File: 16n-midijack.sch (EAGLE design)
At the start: 28 parts

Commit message: Everything on the board.
Now needs routing. Oh boy.
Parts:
- added C1, C2, C3, C4, C5, C6, C7, C8: 100n, rcl:C-EUC0805
- added J1, J10, J11, J12, J13, J14, J15, J16, J2, J3, J4, J5, J6, J7, J8, J9: THONKICONNNEW, MusicThingModular:THONKICONNNEW
- added R10, R14, R15, R19, R20, R24, R25, R29, R30, R34, R35, R39, R40, R44, R5, R9: 5.6K, rcl:R-EU_R0805
- added R11, R13, R16, R18, R21, R23, R26, R28, R31, R33, R36, R38, R41, R43, R6, R8: 10K, rcl:R-EU_R0805
- added R12, R17, R22, R27, R32, R37, R42, R45, R46, R47, R48, R49, R50, R51, R52, R7: 100, rcl:R-EU_R0805
- added U1, U2, U3, U4, U5, U6, U7, U8: MCP6004_SMD, MusicThingModular:MCP6004_SMD
- D1, D2, D3, D4: value DIODE-1N4148 -> DIODESOD123; device SparkFun-DiscreteSemi:DIODE-1N4148 -> foxfield:DIODESOD123
- R1, R2: value (none) -> 220; device SparkFun-Resistors:RESISTORAXIAL-0.3-KIT -> rcl:R-EU_R0805
- R3, R4: device SparkFun-Resistors:RESISTORAXIAL-0.3-KIT -> rcl:R-EU_R0805
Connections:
- new net CV1: J1.TIP, R7.2
- new net CV10: J10.TIP, R48.2
- new net CV11: J11.TIP, R32.2
- new net CV12: J12.TIP, R49.2
- new net CV13: J13.TIP, R37.2
- new net CV14: J14.TIP, R50.2
- new net CV15: J15.TIP, R42.2
- new net CV16: J16.TIP, R51.2
- new net CV2: J2.TIP, R12.2
- new net CV3: J3.TIP, R52.2
- new net CV4: J4.TIP, R45.2
- new net CV5: J5.TIP, R17.2
- new net CV6: J6.TIP, R47.2
- new net CV7: J7.TIP, R22.2
- new net CV8: J8.TIP, R46.2
- new net CV9: J9.TIP, R27.2
- new net N$10: R8.2, R9.2, U1D.+IN
- new net N$11: R17.1, U3C.-IN, U3C.OUT
- new net N$12: R15.2, R16.2, U3C.+IN
- new net N$13: R18.2, R19.2, U3D.+IN
- new net N$14: R22.1, U4C.-IN, U4C.OUT
- new net N$15: R20.2, R21.2, U4C.+IN
- new net N$16: R23.2, R24.2, U4D.+IN
- new net N$17: R27.1, U5C.-IN, U5C.OUT
- new net N$18: R25.2, R26.2, U5C.+IN
- new net N$19: R28.2, R29.2, U5D.+IN
- new net N$20: R32.1, U6C.-IN, U6C.OUT
- new net N$21: R30.2, R31.2, U6C.+IN
- new net N$22: R33.2, R34.2, U6D.+IN
- new net N$23: R37.1, U7C.-IN, U7C.OUT
- new net N$24: R35.2, R36.2, U7C.+IN
- new net N$25: R38.2, R39.2, U7D.+IN
- new net N$256: R12.1, U1D.-IN, U1D.OUT
- new net N$257: R45.1, U2D.-IN, U2D.OUT
- new net N$258: R47.1, U3D.-IN, U3D.OUT
- new net N$259: R46.1, U4D.-IN, U4D.OUT
- new net N$26: R42.1, U8C.-IN, U8C.OUT
- new net N$260: R48.1, U5D.-IN, U5D.OUT
- new net N$261: R49.1, U6D.-IN, U6D.OUT
- new net N$262: R50.1, U7D.-IN, U7D.OUT
- new net N$263: R51.1, U8D.-IN, U8D.OUT
- new net N$27: R40.2, R41.2, U8C.+IN
- new net N$28: R43.2, R44.2, U8D.+IN
- new net N$5: R52.1, U2C.-IN, U2C.OUT
- new net N$6: R10.2, R11.2, U2C.+IN
- new net N$7: R13.2, R14.2, U2D.+IN
- new net N$8: R7.1, U1C.-IN, U1C.OUT
- new net N$9: R5.2, R6.2, U1C.+IN
- new net W0: R5.1, U$17.2, U1B.+IN
- new net W1: R9.1, U$16.2, U1A.+IN
- new net W10: R30.1, U$7.2, U6B.+IN
- new net W11: R34.1, U$6.2, U6A.+IN
- new net W12: R35.1, U$5.2, U7B.+IN
- new net W13: R39.1, U$4.2, U7A.+IN
- new net W14: R40.1, U$3.2, U8B.+IN
- new net W15: R44.1, U$2.2, U8A.+IN
- new net W2: R10.1, U$15.2, U2B.+IN
- new net W3: R14.1, U$14.2, U2A.+IN
- new net W4: R15.1, U$13.2, U3B.+IN
- new net W5: R19.1, U$12.2, U3A.+IN
- new net W6: R20.1, U$11.2, U4B.+IN
- new net W7: R24.1, U$10.2, U4A.+IN
- new net W8: R25.1, U$9.2, U5B.+IN
- new net W9: R29.1, U$8.2, U5A.+IN
- net +3V3: no longer U$10.1, U$11.1, U$12.1, U$13.1, U$14.1, U$15.1, U$16.1, U$17.1, U$2.1, U$3.1, U$4.1, U$5.1, U$6.1, U$7.1, U$8.1, U$9.1
- net +5V: now also C1.1, C2.1, C3.1, C4.1, C5.1, C6.1, C7.1, C8.1, U$10.1, U$11.1, U$12.1, U$13.1, U$14.1, U$15.1, U$16.1, U$17.1, U$2.1, U$3.1, U$4.1, U$5.1, U$6.1, U$7.1, U$8.1, U$9.1, U1P.V+, U2P.V+, U3P.V+, U4P.V+, U5P.V+, U6P.V+, U7P.V+, U8P.V+
- net A0: now also U1B.-IN, U1B.OUT; no longer U$2.2
- net A1: now also U1A.-IN, U1A.OUT; no longer U$3.2
- net A10: now also U6B.-IN, U6B.OUT; no longer U$12.2
- net A11: now also U6A.-IN, U6A.OUT; no longer U$13.2
- net A12: now also U7B.-IN, U7B.OUT; no longer U$14.2
- net A13: now also U7A.-IN, U7A.OUT; no longer U$15.2
- net A14: now also U8B.-IN, U8B.OUT; no longer U$16.2
- net A15: now also U8A.-IN, U8A.OUT; no longer U$17.2
- net A2: now also U2B.-IN, U2B.OUT; no longer U$4.2
- net A3: now also U2A.-IN, U2A.OUT; no longer U$5.2
- net A4: now also U3B.-IN, U3B.OUT; no longer U$6.2
- net A5: now also U3A.-IN, U3A.OUT; no longer U$7.2
- net A6: now also U4B.-IN, U4B.OUT; no longer U$8.2
- net A7: now also U4A.-IN, U4A.OUT; no longer U$9.2
- net A8: now also U5B.-IN, U5B.OUT; no longer U$10.2
- net A9: now also U5A.-IN, U5A.OUT; no longer U$11.2
- net GND: now also C1.2, C2.2, C3.2, C4.2, C5.2, C6.2, C7.2, C8.2, J1.SLEEVE, J10.SLEEVE, J11.SLEEVE, J12.SLEEVE, J13.SLEEVE, J14.SLEEVE, J15.SLEEVE, J16.SLEEVE, J2.SLEEVE, J3.SLEEVE, J4.SLEEVE, J5.SLEEVE, J6.SLEEVE, J7.SLEEVE, J8.SLEEVE, J9.SLEEVE, R11.1, R13.1, R16.1, R18.1, R21.1, R23.1, R26.1, R28.1, R31.1, R33.1, R36.1, R38.1, R41.1, R43.1, R6.1, R8.1, U1P.V-, U2P.V-, U3P.V-, U4P.V-, U5P.V-, U6P.V-, U7P.V-, U8P.V-

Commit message: Boom. Routed.
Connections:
- net A4: now also U$1.18/A4/T/SDA0
- net A5: now also U$1.19/A5/T/SCL0
- net SCL: now also U$1.29/A18/SCL1; no longer U$1.19/A5/T/SCL0
- net SDA: now also U$1.30/A19/SDA1; no longer U$1.18/A4/T/SDA0
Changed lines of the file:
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@@
 <net name="SDA" class="0">
-<segment>
-<pinref part="U$1" gate="G$1" pin="18/A4/T/SDA0"/>
-<wire x1="78.74" y1="91.44" x2="81.28" y2="91.44" width="0.1524" layer="91"/>
-<label x="77.47" y="92.71" size="1.778" layer="95" rot="R180"/>
-<wire x1="78.74" y1="91.44" x2="68.58" y2="91.44" width="0.1524" layer="91"/>
-<label x="68.58" y="91.44" size="1.27" layer="95" rot="R180" xref="yes"/>
-</segment>
 <segment>
 <pinref part="II" gate="A" pin="2"/>
@@
 <junction x="289.56" y="111.76"/>
 </segment>
+<segment>
+<pinref part="U$1" gate="G$1" pin="30/A19/SDA1"/>
+<wire x1="127" y1="88.9" x2="129.54" y2="88.9" width="0.1524" layer="91"/>
+<label x="129.54" y="88.9" size="1.778" layer="95"/>
+</segment>
 </net>
 <net name="SCL" class="0">
-<segment>
-<pinref part="U$1" gate="G$1" pin="19/A5/T/SCL0"/>
-<wire x1="78.74" y1="88.9" x2="81.28" y2="88.9" width="0.1524" layer="91"/>
-<label x="77.47" y="90.17" size="1.778" layer="95" rot="R180"/>
-<wire x1="78.74" y1="88.9" x2="68.58" y2="88.9" width="0.1524" layer="91"/>
-<label x="68.58" y="88.9" size="1.27" layer="95" rot="R180" xref="yes"/>
-</segment>
 <segment>
 <pinref part="II" gate="A" pin="3"/>
@@
 <junction x="269.24" y="109.22"/>
 </segment>
+<segment>
+<pinref part="U$1" gate="G$1" pin="29/A18/SCL1"/>
+<wire x1="127" y1="86.36" x2="129.54" y2="86.36" width="0.1524" layer="91"/>
+<label x="129.54" y="86.36" size="1.778" layer="95"/>
+</segment>
 </net>
 <net name="W7" class="0">
@@
 </segment>
 </net>
+<net name="A4" class="0">
+<segment>
+<pinref part="U$1" gate="G$1" pin="18/A4/T/SDA0"/>
+<wire x1="78.74" y1="91.44" x2="81.28" y2="91.44" width="0.1524" layer="91"/>
+<label x="77.47" y="92.71" size="1.778" layer="95" rot="R180"/>
+<wire x1="78.74" y1="91.44" x2="68.58" y2="91.44" width="0.1524" layer="91"/>
+<label x="68.58" y="91.44" size="1.27" layer="95" rot="R180"/>
+</segment>
+</net>
+<net name="A5" class="0">
+<segment>
+<pinref part="U$1" gate="G$1" pin="19/A5/T/SCL0"/>
+<wire x1="78.74" y1="88.9" x2="81.28" y2="88.9" width="0.1524" layer="91"/>
+<label x="77.47" y="90.17" size="1.778" layer="95" rot="R180"/>
+<wire x1="78.74" y1="88.9" x2="68.58" y2="88.9" width="0.1524" layer="91"/>
+<label x="68.58" y="88.9" size="1.27" layer="95" rot="R180"/>
+</segment>
+</net>

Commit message: New layout with horizontal jacks.
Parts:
- J1, J10, J11, J12, J13, J14, J15, J16, J2, J3, J4, J5, J6, J7, J8, J9: value THONKICONNNEW -> PJ302M; device MusicThingModular:THONKICONNNEW -> pj302m:PJ302M
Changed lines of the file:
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@@
 <part name="SUPPLY16" library="supply2" library_urn="urn:adsk.eagle:library:372" deviceset="+5V" device=""/>
 <part name="SUPPLY17" library="supply2" library_urn="urn:adsk.eagle:library:372" deviceset="+5V" device=""/>
-<part name="J1" library="MusicThingModular" deviceset="THONKICONN" device="NEW"/>
+<part name="J1" library="pj302m" deviceset="PJ302M" device=""/>
 <part name="SUPPLY18" library="supply2" library_urn="urn:adsk.eagle:library:372" deviceset="GND" device=""/>
-<part name="J2" library="MusicThingModular" deviceset="THONKICONN" device="NEW"/>
+<part name="J2" library="pj302m" deviceset="PJ302M" device=""/>
 <part name="SUPPLY19" library="supply2" library_urn="urn:adsk.eagle:library:372" deviceset="GND" device=""/>
-<part name="J3" library="MusicThingModular" deviceset="THONKICONN" device="NEW"/>
+<part name="J3" library="pj302m" deviceset="PJ302M" device=""/>
 <part name="SUPPLY20" library="supply2" library_urn="urn:adsk.eagle:library:372" deviceset="GND" device=""/>
-<part name="J4" library="MusicThingModular" deviceset="THONKICONN" device="NEW"/>
+<part name="J4" library="pj302m" deviceset="PJ302M" device=""/>
 <part name="SUPPLY21" library="supply2" library_urn="urn:adsk.eagle:library:372" deviceset="GND" device=""/>
-<part name="J5" library="MusicThingModular" deviceset="THONKICONN" device="NEW"/>
+<part name="J5" library="pj302m" deviceset="PJ302M" device=""/>
 <part name="SUPPLY22" library="supply2" library_urn="urn:adsk.eagle:library:372" deviceset="GND" device=""/>
-<part name="J6" library="MusicThingModular" deviceset="THONKICONN" device="NEW"/>
+<part name="J6" library="pj302m" deviceset="PJ302M" device=""/>
 <part name="SUPPLY23" library="supply2" library_urn="urn:adsk.eagle:library:372" deviceset="GND" device=""/>
-<part name="J7" library="MusicThingModular" deviceset="THONKICONN" device="NEW"/>
+<part name="J7" library="pj302m" deviceset="PJ302M" device=""/>
 <part name="SUPPLY24" library="supply2" library_urn="urn:adsk.eagle:library:372" deviceset="GND" device=""/>
-<part name="J8" library="MusicThingModular" deviceset="THONKICONN" device="NEW"/>
+<part name="J8" library="pj302m" deviceset="PJ302M" device=""/>
 <part name="SUPPLY25" library="supply2" library_urn="urn:adsk.eagle:library:372" deviceset="GND" device=""/>
-<part name="J9" library="MusicThingModular" deviceset="THONKICONN" device="NEW"/>
+<part name="J9" library="pj302m" deviceset="PJ302M" device=""/>
 <part name="SUPPLY26" library="supply2" library_urn="urn:adsk.eagle:library:372" deviceset="GND" device=""/>
-<part name="J10" library="MusicThingModular" deviceset="THONKICONN" device="NEW"/>
+<part name="J10" library="pj302m" deviceset="PJ302M" device=""/>
 <part name="SUPPLY27" library="supply2" library_urn="urn:adsk.eagle:library:372" deviceset="GND" device=""/>
-<part name="J11" library="MusicThingModular" deviceset="THONKICONN" device="NEW"/>
+<part name="J11" library="pj302m" deviceset="PJ302M" device=""/>
 <part name="SUPPLY28" library="supply2" library_urn="urn:adsk.eagle:library:372" deviceset="GND" device=""/>
-<part name="J12" library="MusicThingModular" deviceset="THONKICONN" device="NEW"/>
+<part name="J12" library="pj302m" deviceset="PJ302M" device=""/>
 <part name="SUPPLY29" library="supply2" library_urn="urn:adsk.eagle:library:372" deviceset="GND" device=""/>
-<part name="J13" library="MusicThingModular" deviceset="THONKICONN" device="NEW"/>
+<part name="J13" library="pj302m" deviceset="PJ302M" device=""/>
 <part name="SUPPLY30" library="supply2" library_urn="urn:adsk.eagle:library:372" deviceset="GND" device=""/>
-<part name="J14" library="MusicThingModular" deviceset="THONKICONN" device="NEW"/>
+<part name="J14" library="pj302m" deviceset="PJ302M" device=""/>
 <part name="SUPPLY31" library="supply2" library_urn="urn:adsk.eagle:library:372" deviceset="GND" device=""/>
-<part name="J15" library="MusicThingModular" deviceset="THONKICONN" device="NEW"/>
+<part name="J15" library="pj302m" deviceset="PJ302M" device=""/>
 <part name="SUPPLY32" library="supply2" library_urn="urn:adsk.eagle:library:372" deviceset="GND" device=""/>
-<part name="J16" library="MusicThingModular" deviceset="THONKICONN" device="NEW"/>
+<part name="J16" library="pj302m" deviceset="PJ302M" device=""/>
 <part name="SUPPLY33" library="supply2" library_urn="urn:adsk.eagle:library:372" deviceset="GND" device=""/>
 <part name="U1" library="MusicThingModular" deviceset="MCP6004" device="_SMD"/>

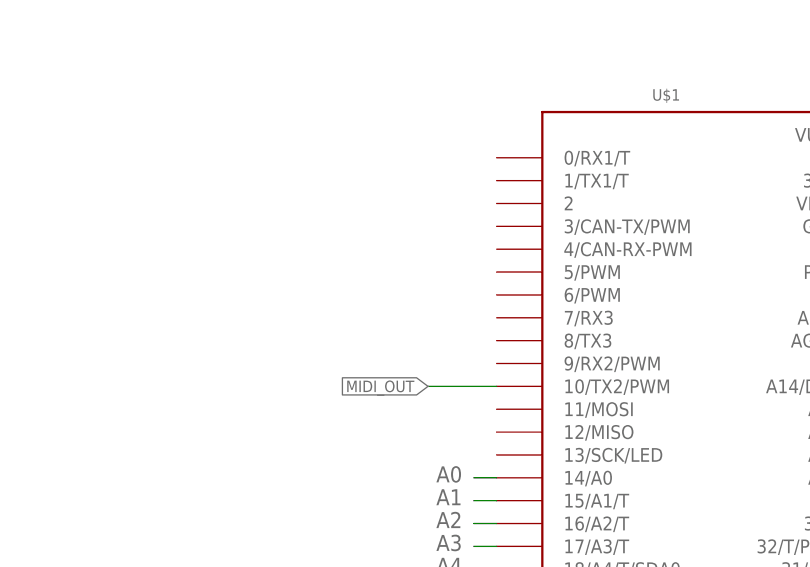
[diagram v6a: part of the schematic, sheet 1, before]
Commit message: MIDI has to go to serial TX.
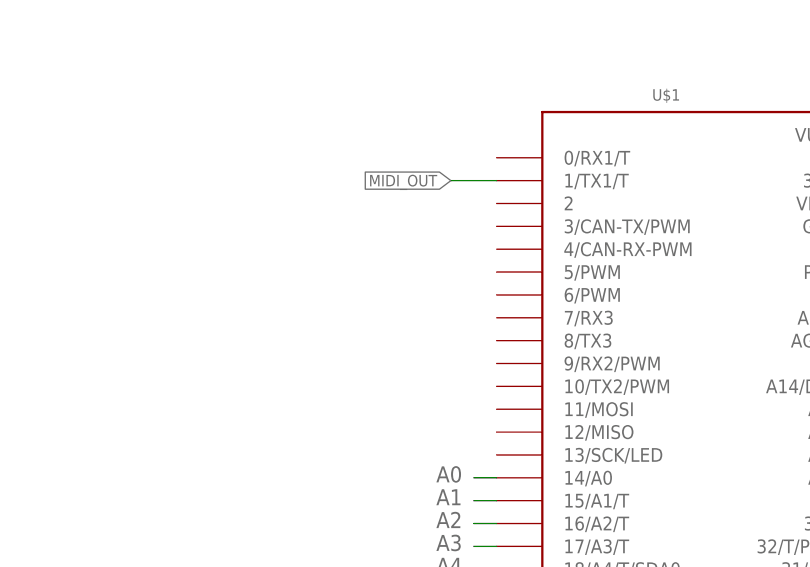
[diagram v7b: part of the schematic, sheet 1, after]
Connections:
- net MIDI_OUT: now also U$1.1/TX1/T; no longer U$1.10/TX2/PWM
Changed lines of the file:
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@@
 </segment>
 <segment>
-<pinref part="U$1" gate="G$1" pin="10/TX2/PWM"/>
-<wire x1="81.28" y1="111.76" x2="73.66" y2="111.76" width="0.1524" layer="91"/>
-<label x="73.66" y="111.76" size="1.27" layer="95" rot="R180" xref="yes"/>
+<pinref part="U$1" gate="G$1" pin="1/TX1/T"/>
+<wire x1="81.28" y1="134.62" x2="76.2" y2="134.62" width="0.1524" layer="91"/>
+<label x="76.2" y="134.62" size="1.27" layer="95" rot="R180" xref="yes"/>
 </segment>
 </net>
